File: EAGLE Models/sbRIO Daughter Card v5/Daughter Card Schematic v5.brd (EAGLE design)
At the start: 101.6 x 81.3 mm, 68 parts, among them IC1 BTS716G, IC2 BTS716G, IC3 BTS716G, Q7 MMBT4403-7-F, Q8 MMBT4403-7-F, U2 ADXL345, U3 L3G4200D, X1 5566-2

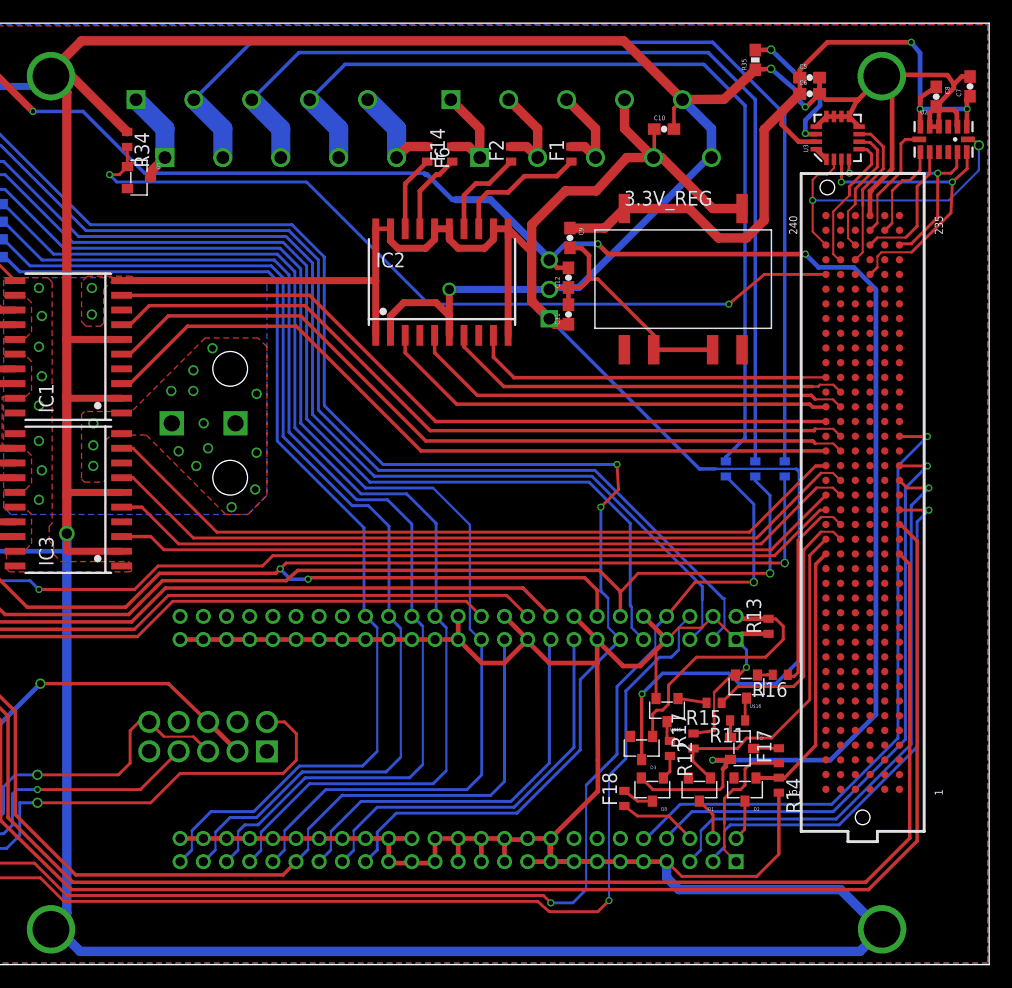
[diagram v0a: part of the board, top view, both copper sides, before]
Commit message: Made layout pass DRC
also added level shifted inputs for wheel speeds
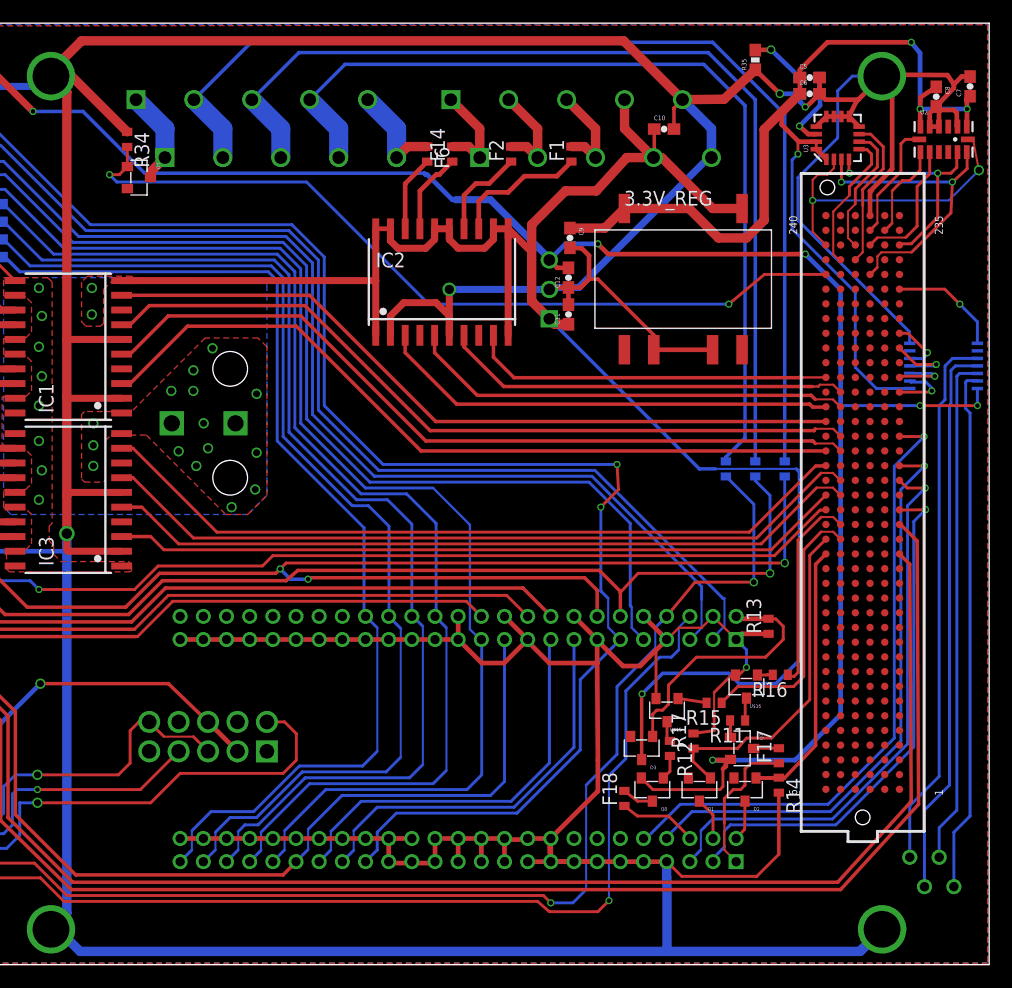
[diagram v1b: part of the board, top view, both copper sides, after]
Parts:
- added U1: (no value), SparkFun-DigitalIC:TSSOP14
- added X2: (no value), con-amp:FTOP-4
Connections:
- removed net N$24: U$3.163
- new net DIO80: U$3.235
- new net DIO84: U$3.199
- new net DIO88: U$3.163, U1.2
- new net WS1: U1.13, X2.1
- new net WS2: U1.12, X2.2
- new net WS3: U1.11, X2.3
- new net WS4: U1.10, X2.4
- net 3.3V: now also U1.1
- net 5V: now also U1.14
- net DIO83: now also U1.8
- net DIO85: now also U1.5
- net DIO86: now also U1.4
- net DIO87: now also U1.3
- net GND: now also U1.7
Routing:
- net WS3: track 0.00 -> 48.0 mm
- net WS4: track 0.00 -> 46.7 mm
- net WS1: track 0.00 -> 45.4 mm
- net WS2: track 0.00 -> 44.0 mm
- net 3.3V: track 69.2 -> 97.3 mm, vias 3 -> 4
- net GND: track 623.9 -> 643.9 mm
- net DIO83: track 0.00 -> 9.76 mm, vias 0 -> 1
- net 5V: track 191.7 -> 198.9 mm, vias 4 -> 6
- net DIO86: track 0.00 -> 6.10 mm, vias 0 -> 1
- net DIO87: track 0.00 -> 5.34 mm, vias 0 -> 1
- net DIO88: track 0.00 -> 5.24 mm, vias 0 -> 1
- net DIO85: track 0.00 -> 4.92 mm, vias 0 -> 1
- net DIO94: track 136.9 -> 135.3 mm
- net DIO95: track 127.3 -> 125.7 mm
- net DIO92: track 49.9 -> 49.2 mm
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
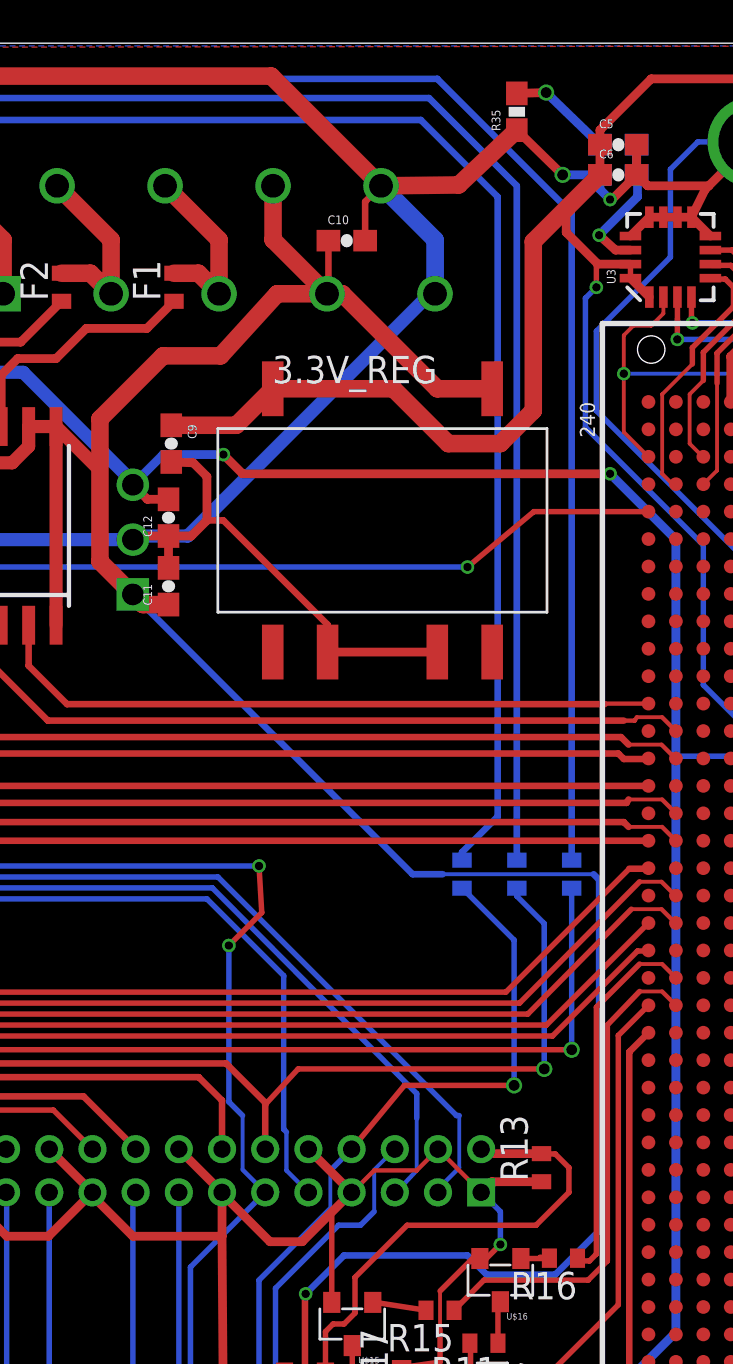
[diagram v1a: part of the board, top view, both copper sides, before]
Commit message: Added values for fuses
also rerouted a trace which was unnecesarily long
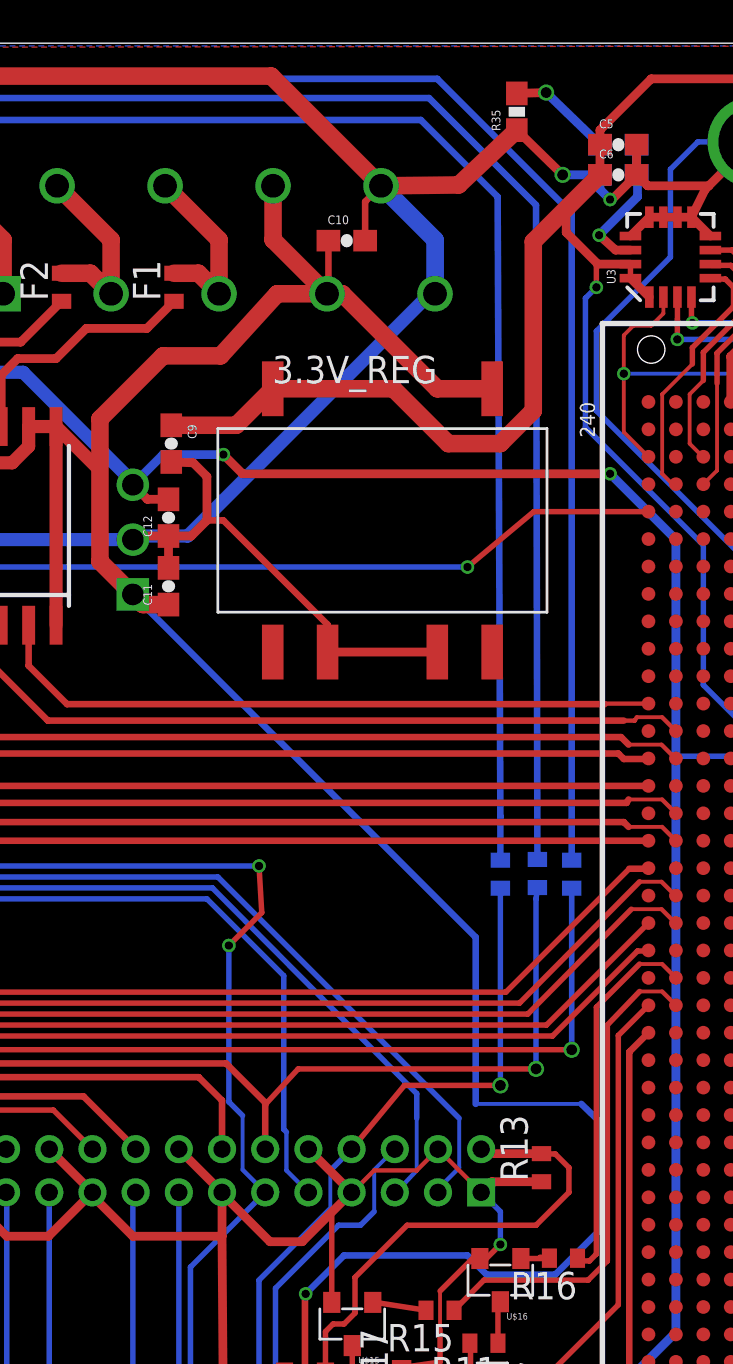
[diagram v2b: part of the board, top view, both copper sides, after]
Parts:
- F1, F14, F2, F6, F7, F8: value (none) -> 0.25A PTC
- F10, F16: value (none) -> 0.5A PTC
- F15, F20, F21, F22: value (none) -> 0.01A PTC
- F17, F18, F19, F9: value (none) -> 1A PTC
- F3, F4, F5: value (none) -> 1mA PTC
- moved F5 1.78 mm to (80.6, 42.8)
- moved F4 0.95 mm to (82.4, 42.8)
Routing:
- net 12V: track 193.7 -> 191.7 mm
- net AI2: track 102.4 -> 100.8 mm
- net AI3: track 86.0 -> 85.2 mm
- net N$43: track 77.8 -> 77.1 mm

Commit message: PTC fuses dont exisist in 0402, made all fuses 0603 instead
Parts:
- F1, F10, F14, F15, F16, F17, F18, F19, F2, F20, F21, F22, F3, F4, F5, F6, F7, F8, F9: device resistor:R0402 -> resistor:R0603

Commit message: some of the 0603 PTC fuses were not possible to lay on board well
replaced with normal fuses
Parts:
- F15, F20, F21, F22: device resistor:R0603 -> resistor:R0402
- moved F8 2.04 mm to (10.4, 16.4)
- moved F16 1.40 mm to (7.11, 77.2)
- moved F7 1.02 mm to (11.9, 21.1)
- moved F10 0.89 mm to (12.4, 49.7)
- moved F17 0.57 mm to (83.9, 18.3)
- moved F18 0.52 mm to (70.0, 14.9)
- moved D6 0.18 mm to (9.40, 21.0)
- moved F9 0.13 mm to (14.9, 44.6)
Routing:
- net 5V: track 198.9 -> 202.4 mm
- net N$13: track 4.26 -> 2.24 mm
- net AMS_OK: track 1.93 -> 3.72 mm
- net IMD_OK: track 1.53 -> 2.54 mm
- net N$14: track 7.12 -> 6.11 mm
- net N$17: track 2.58 -> 1.69 mm
- net N$56: track 2.19 -> 2.86 mm
- net DIO14: track 25.2 -> 25.8 mm
- net N$55: track 12.7 -> 13.2 mm

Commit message: changed step-down diodes into linear regulators
also made schematic far more readable, and removed some unnecessary
outputs on TUB_CONN
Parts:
- removed D1, D2, D4, D5, D6: MMBZ5238B-7-F, formula electric:SOT-23-3
- removed F10: 0.5A PTC, resistor:R0603
- removed F7, F8: 0.25A PTC, resistor:R0603
- removed F9: 1A PTC, resistor:R0603
- removed R14, R17, R34, R8, R9: 10k, resistor:R0402
- added C16, C17, C18, C19, C20: 1uF, SparkFun-Passives:0603-CAP
- added R1, R2, R3, R4, R5: 10k, resistor:R0402
- added U$1, U$4, U$5, U$6, U$7: MIC5225-3.3YM5-TR, formula electric:SOT-23-3
- renumbered X2 to WHEEL
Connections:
- net AI3 renamed BRAKE_PRESS_IN_1
- net AI4 renamed BRAKE_PRESS_IN_2
- net BSPD5 renamed THROTTLE_OK_OUT
- net PO1 renamed ACCUMULATOR_FANS
- net THROTTLE_1 renamed THROTTLE_IN_1
- net THROTTLE_2 renamed THROTTLE_IN_2
- removed net AMS_OK: D6.P$1, F8.2
- removed net IMD_OK: D5.P$1, F7.2
- removed net N$1: D2.P$1, SBRIO_AUX.P$2
- removed net N$13: ACCUMULATOR_CONN.7, F8.1
- removed net N$14: ACCUMULATOR_CONN.8, F7.1
- removed net N$16: F9.1, TUB_CONN.3
- removed net N$17: F10.1, TUB_CONN.1
- removed net N$2: D1.P$1, SBRIO_AUX.P$4
- removed net N$42: BSPD_CONN.1, BSPD_CONN.2, D4.P$1
- removed net N$55: F17.1, SBRIO_AUX.P$1
- removed net N$59: F18.1, SBRIO_AUX.P$6
- new net 5V_IO_1: F17.1
- new net AMS_OK_IN: ACCUMULATOR_CONN.7, R1.1, U$4.P$3
- new net BSPD_OK_IN: BSPD_CONN.1, BSPD_CONN.2, R2.1, U$5.P$3
- new net DC_DC_DISABLE: F18.1
- new net E-STOP_OK: R3.1, U$6.P$3
- new net IMD_OK_IN: ACCUMULATOR_CONN.8, R5.1, U$1.P$3
- new net LATCH_OK: R4.1, U$7.P$3
- net 12V: no longer F9.2
- net 5V: no longer F10.2
- net CAN_GND: now also TUB_CONN.10
- net DIO1: now also C16.1, U$7.P$2; no longer D4.P$2, R34.2
- net DIO13: now also C17.1, U$6.P$2; no longer D1.P$2, R17.1
- net DIO14: now also C18.1, U$5.P$2; no longer D2.P$2, R14.1
- net DIO94: now also C19.1, U$4.P$2; no longer D6.P$2, R9.1
- net DIO95: now also C20.1, U$1.P$2; no longer D5.P$2, R8.2
- net GND: now also C16.2, C17.2, C18.2, C19.2, C20.2, R1.2, R2.2, R3.2, R4.2, R5.2, U$1.P$1, U$4.P$1, U$5.P$1, U$6.P$1, U$7.P$1; no longer R14.2, R17.2, R34.1, R8.1, R9.2, TUB_CONN.10
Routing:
- net GND: track 643.9 -> 613.5 mm
- net N$55: track 13.2 -> 0.00 mm
- net N$42: track 8.28 -> 0.00 mm
- net BSPD_OK_IN: track 0.00 -> 7.80 mm
- net N$59: track 7.11 -> 0.00 mm
- net N$14: track 6.11 -> 0.00 mm
- net DIO14: track 25.8 -> 20.3 mm
- net DIO94: track 135.1 -> 130.4 mm
- net DIO13: track 29.2 -> 24.5 mm
- net AMS_OK: track 3.72 -> 0.00 mm
- net N$2: track 3.71 -> 0.00 mm
- net N$1: track 3.51 -> 0.00 mm
- net DIO1: track 70.9 -> 68.3 mm
- net IMD_OK: track 2.54 -> 0.00 mm
- net N$13: track 2.24 -> 0.00 mm
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
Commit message: indermediate commit during layout
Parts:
- removed F19: 1A PTC, resistor:R0603
- moved C16 125.3 mm to (24.6, 75.9), turned to 90 degrees
- moved R4 120.1 mm to (27.8, 77.7), turned to 90 degrees
- moved U$7 96.9 mm to (26.2, 71.6), turned to 270 degrees
- moved U$6 90.3 mm to (3.94, 73.7), turned to 90 degrees
- moved R2 55.9 mm to (18.9, 18.3), flipped to the bottom, turned to 180 degrees
- moved R1 47.6 mm to (9.27, 20.2), turned to 90 degrees
- moved U$5 42.0 mm to (18.5, 15.2), flipped to the bottom, turned to 270 degrees
- moved U$4 40.1 mm to (8.13, 22.2), turned to 180 degrees
- moved R36 3.68 mm to (7.37, 45.8)
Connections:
- new net N$1: TUB_CONN.3
- new net N$2: TUB_CONN.1
- net 12V: no longer F19.1
- net AI11: no longer AIO_PO_CONN.4
- net AI15: no longer AIO_PO_CONN.8
- net AMS_OK_IN: now also U$4.P$1; no longer U$4.P$3
- net BSPD_OK_IN: now also R4.1, U$7.P$1; no longer R2.1, U$5.P$3
- net DIO1: now also U$7.P$3; no longer U$7.P$2
- net DIO13: now also U$6.P$3; no longer U$6.P$2
- net DIO14: now also U$5.P$3; no longer U$5.P$2
- net DIO94: now also U$4.P$3; no longer U$4.P$2
- net DIO95: now also U$1.P$3; no longer U$1.P$2
- net E-STOP_OK: now also AIO_PO_CONN.4, U$6.P$1; no longer U$6.P$3
- net GND: now also U$1.P$2, U$4.P$2, U$5.P$2, U$6.P$2, U$7.P$2; no longer AIO_PO_CONN.1, U$1.P$1, U$4.P$1, U$5.P$1, U$6.P$1, U$7.P$1
- net IMD_OK_IN: now also R2.1, U$5.P$1; no longer R5.1, U$1.P$3
- net LATCH_OK: now also AIO_PO_CONN.8, R5.1, U$1.P$1; no longer R4.1, U$7.P$3
- net N$29: no longer F19.2
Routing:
- net GND: track 613.5 -> 656.2 mm, vias 10 -> 11
- net DIO7: track 39.8 -> 0.04 mm
- net DIO39: track 38.5 -> 2.46 mm
- net DIO38: track 35.3 -> 2.77 mm
- net 12V: track 189.4 -> 157.9 mm
- net DIO6: track 31.3 -> 0.00 mm
- net 5V: track 201.5 -> 170.4 mm
- net DIO94: track 130.4 -> 109.8 mm
- net DIO95: track 124.6 -> 105.1 mm
- net DIO12: track 112.2 -> 102.3 mm
- net DIO1: track 68.3 -> 74.9 mm
- net IMD_OK_IN: track 0.00 -> 6.59 mm
- net DIO8: track 65.3 -> 71.6 mm
- net DIO40: track 67.6 -> 73.6 mm
- net DIO14: track 20.3 -> 26.0 mm, vias 0 -> 1
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
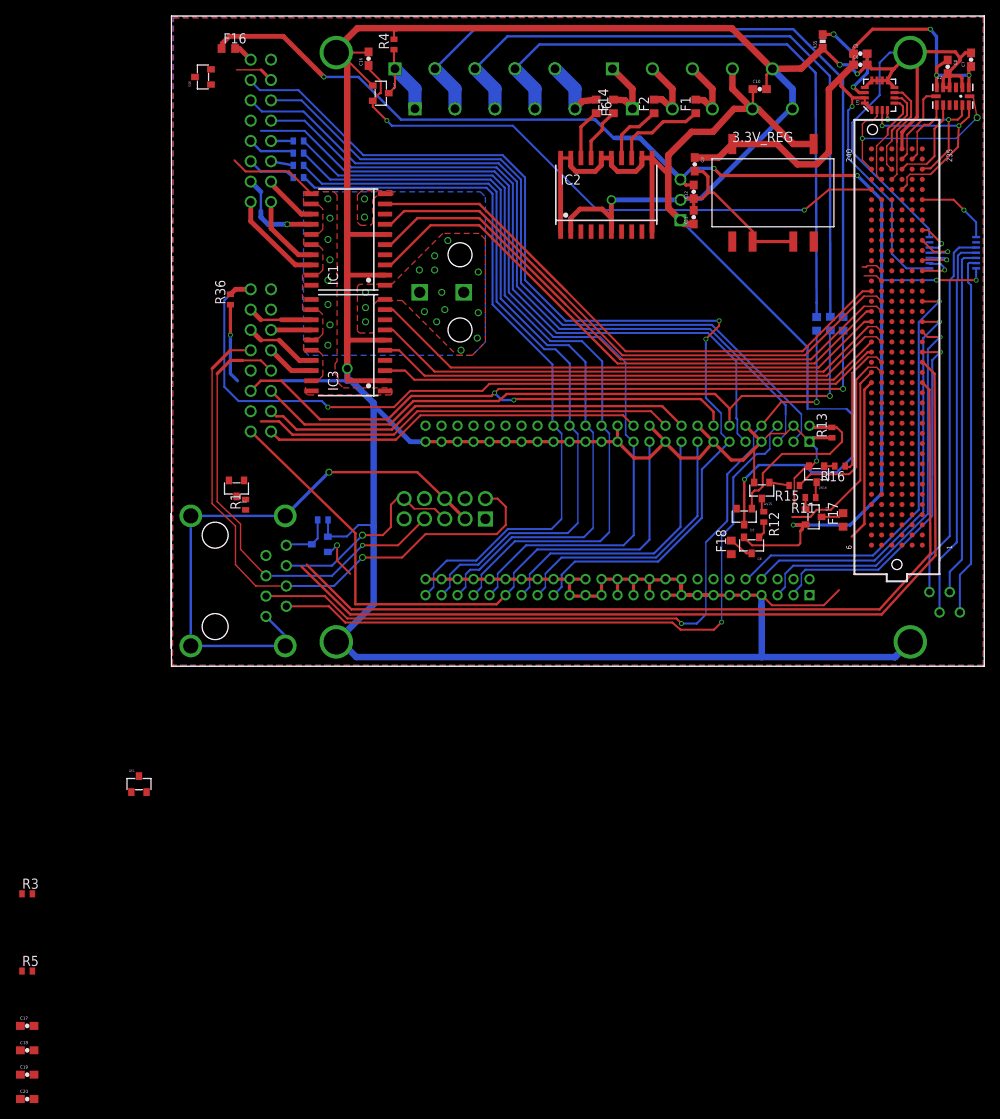
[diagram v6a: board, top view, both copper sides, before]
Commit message: Made board pass DRC
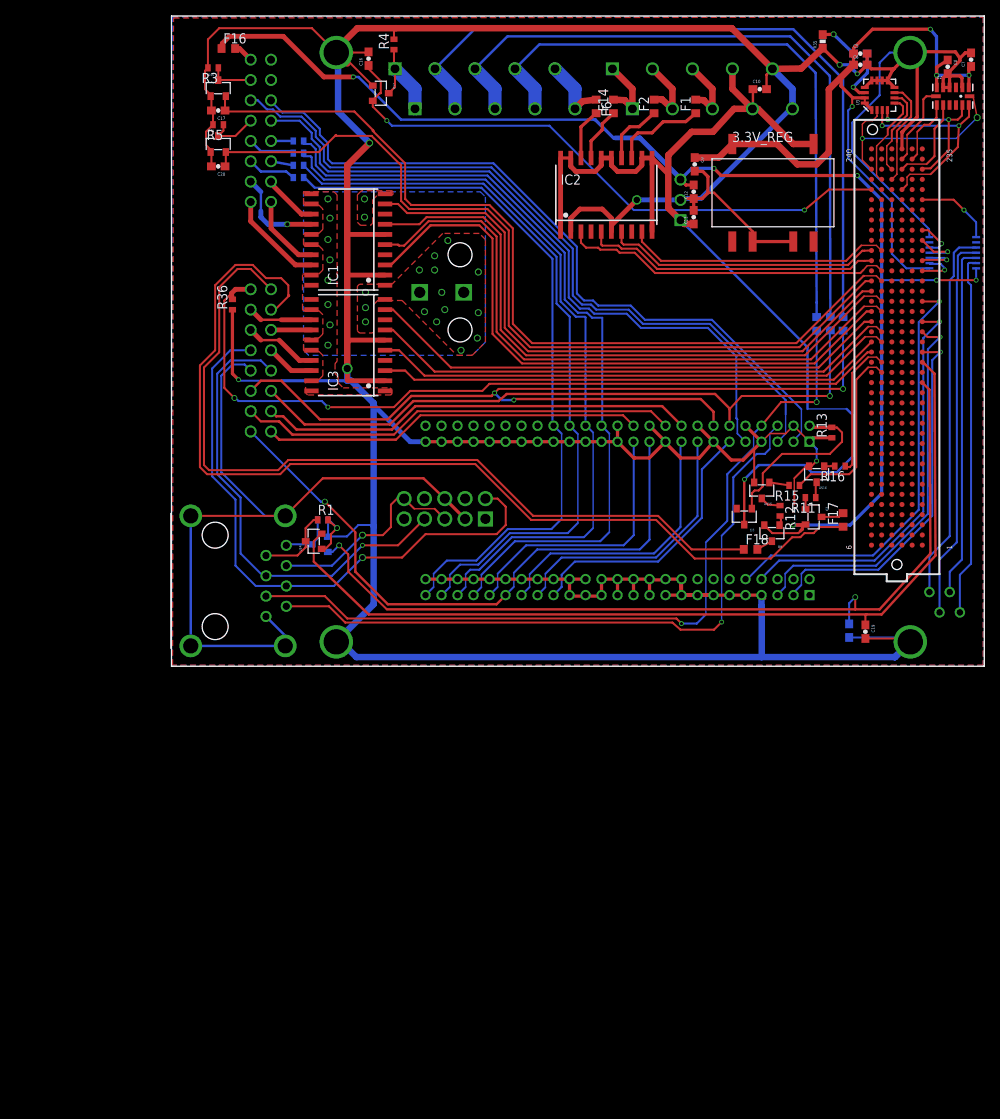
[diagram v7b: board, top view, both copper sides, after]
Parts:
- moved C20 119.0 mm to (5.84, 62.5), turned to 180 degrees
- moved C19 118.5 mm to (86.7, 4.32), turned to 270 degrees
- moved C17 116.9 mm to (5.84, 69.5), turned to 180 degrees
- moved C18 115.4 mm to (84.7, 4.45), flipped to the bottom, turned to 270 degrees
- moved R5 108.5 mm to (5.84, 67.7), turned to 180 degrees
- moved R3 105.8 mm to (5.21, 74.8), turned to 180 degrees
- moved U$1 80.6 mm to (5.84, 65.3)
- moved U$4 11.7 mm to (17.8, 15.6), turned to 90 degrees
- moved R1 9.84 mm to (18.9, 18.3), turned to 0 degrees
- moved Q8 2.96 mm to (75.1, 16.6)
- moved F18 2.43 mm to (72.4, 14.6), turned to 0 degrees
- moved U$6 2.36 mm to (5.84, 72.3), turned to 0 degrees
- moved R12 2.17 mm to (76.1, 19.4)
- moved R36 0.68 mm to (7.62, 45.2)
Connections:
- removed net N$1: TUB_CONN.3
- removed net N$2: TUB_CONN.1
- net 5V_IO_1: now also TUB_CONN.3
- net DC_DC_DISABLE: now also TUB_CONN.1
- net DIO13: no longer C17.1, U$6.P$3
- net DIO14: no longer C18.1, U$5.P$3
- net DIO37: now also IC2.9
- net DIO38: now also IC2.3; no longer IC2.7
- net DIO39: now also C17.1, U$6.P$3; no longer IC2.5
- net DIO5: now also IC2.7
- net DIO6: now also IC2.5; no longer IC2.9
- net DIO7: now also C20.1, U$1.P$3; no longer IC2.3
- net DIO95: now also C18.1, U$5.P$3; no longer C20.1, U$1.P$3
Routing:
- net 5V_IO_1: track 0.00 -> 127.0 mm
- net DIO7: track 0.04 -> 107.5 mm
- net DIO39: track 2.46 -> 109.5 mm
- net DC_DC_DISABLE: track 0.00 -> 104.4 mm
- net AI11: track 129.9 -> 34.4 mm, vias 2 -> 0
- net AI15: track 109.6 -> 33.8 mm
- net GND: track 656.2 -> 703.8 mm, vias 11 -> 12
- net DIO38: track 2.77 -> 41.2 mm
- net DIO6: track 0.00 -> 37.1 mm
- net DIO5: track 0.00 -> 34.5 mm
- net DIO37: track 0.00 -> 33.3 mm
- net CAN_GND: track 71.7 -> 98.0 mm, vias 1 -> 0
- net DIO14: track 26.0 -> 0.00 mm, vias 1 -> 0
- net DIO13: track 24.5 -> 0.00 mm
- net 12V: track 157.9 -> 146.5 mm
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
